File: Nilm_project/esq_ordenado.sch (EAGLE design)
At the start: 37 parts, among them IC1 LM1117IMPX-3.3, J4 10103594-0001LF, Q1 SMD-TRANSISTORS-NPN-25V-500MW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, Q2 SMD-TRANSISTORS-NPN-25V-500MW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, U1 ESP-32S, U2 CP2102-GM, U3 TPD2S017DBVR, U4 SP0503BAHT

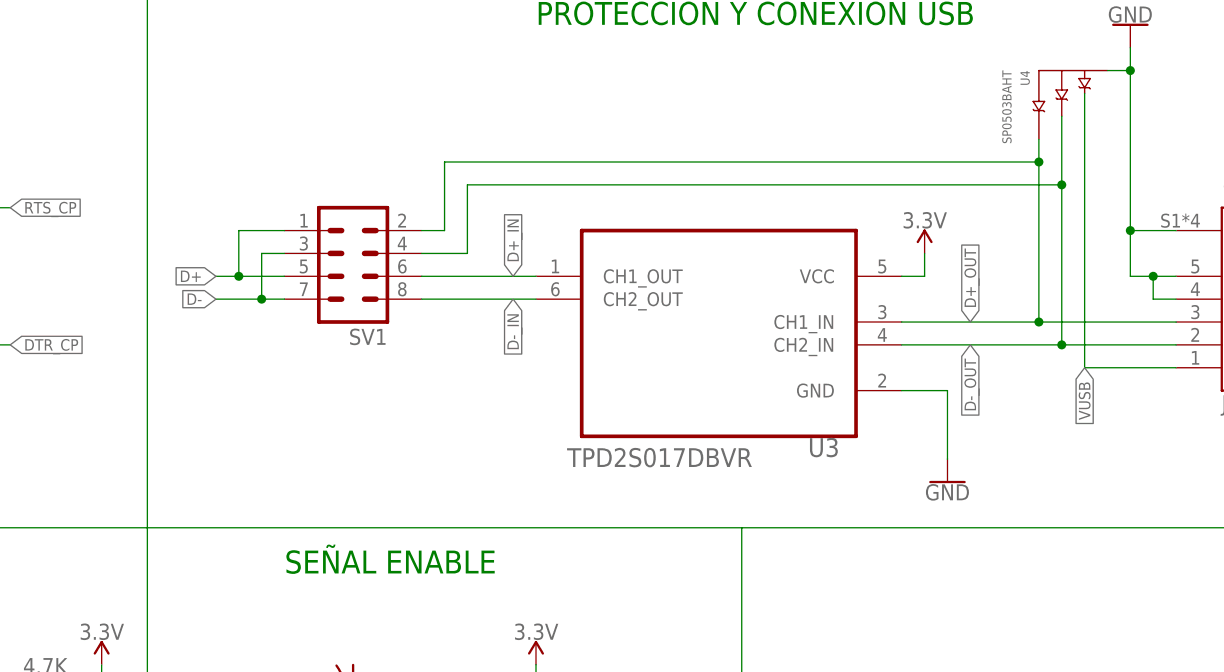
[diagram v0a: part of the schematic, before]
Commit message: Adicionando Datasheet TPD2S017 y conexiones entre D+ y D- a la regleta
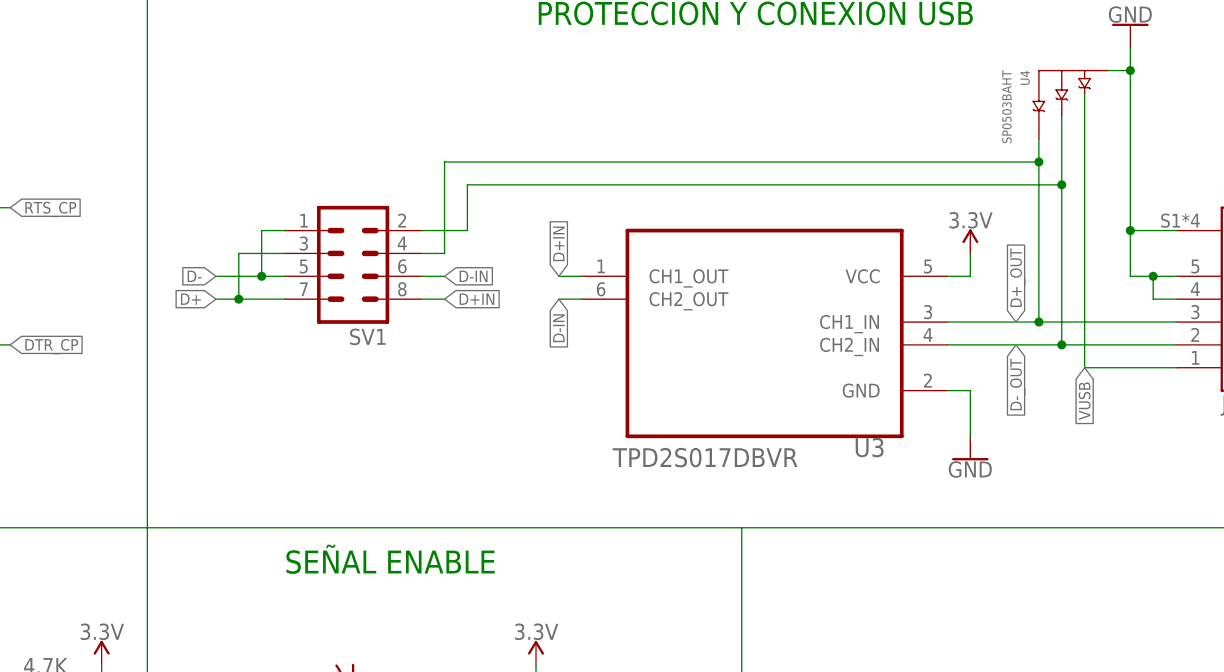
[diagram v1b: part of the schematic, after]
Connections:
- removed net D+_IN: SV1.6, U3.CH1_OUT
- removed net D-_IN: SV1.8, U3.CH2_OUT
- new net D+IN: SV1.8, U3.CH1_OUT
- new net D-IN: SV1.6, U3.CH2_OUT
- net D+: now also SV1.3, SV1.7; no longer SV1.1, SV1.5
- net D+_OUT: now also SV1.4; no longer SV1.2
- net D-: now also SV1.1, SV1.5; no longer SV1.3, SV1.7
- net D-_OUT: now also SV1.2; no longer SV1.4
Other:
- moved on the sheet: U3
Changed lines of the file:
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@@
 <attribute name="NAME" x="214.63" y="189.738" size="1.778" layer="95" rot="R180"/>
 </instance>
-<instance part="U3" gate="A" x="251.46" y="193.04" smashed="yes" rot="MR0">
-<attribute name="NAME" x="264.882759375" y="175.5093" size="2.086959375" layer="95" ratio="10" rot="SMR0"/>
-<attribute name="VALUE" x="255.199990625" y="174.391" size="2.08625" layer="96" ratio="10" rot="SMR0"/>
+<instance part="U3" gate="A" x="256.54" y="193.04" smashed="yes" rot="MR0">
+<attribute name="NAME" x="269.962759375" y="175.5093" size="2.086959375" layer="95" ratio="10" rot="SMR0"/>
+<attribute name="VALUE" x="260.279990625" y="174.391" size="2.08625" layer="96" ratio="10" rot="SMR0"/>
 </instance>
 <instance part="U4" gate="G$1" x="289.56" y="215.9" smashed="yes" rot="R180">
@@
 <attribute name="VALUE" x="282.9587" y="218.460509375" size="1.0162" layer="96" rot="R270"/>
 </instance>
-<instance part="SUPPLY10" gate="G$1" x="274.32" y="198.12" smashed="yes">
-<attribute name="VALUE" x="274.32" y="200.914" size="1.778" layer="96" align="bottom-center"/>
-</instance>
-<instance part="GND21" gate="1" x="276.86" y="172.72" smashed="yes">
-<attribute name="VALUE" x="276.86" y="172.466" size="1.778" layer="96" align="top-center"/>
+<instance part="SUPPLY10" gate="G$1" x="279.4" y="198.12" smashed="yes">
+<attribute name="VALUE" x="279.4" y="200.914" size="1.778" layer="96" align="bottom-center"/>
+</instance>
+<instance part="GND21" gate="1" x="279.4" y="175.26" smashed="yes">
+<attribute name="VALUE" x="279.4" y="175.006" size="1.778" layer="96" align="top-center"/>
 </instance>
 <instance part="GND22" gate="1" x="297.18" y="223.52" smashed="yes" rot="R180">
@@
 <segment>
 <pinref part="U3" gate="A" pin="VCC"/>
-<wire x1="271.78" y1="195.58" x2="274.32" y2="195.58" width="0.1524" layer="91"/>
-<wire x1="274.32" y1="195.58" x2="274.32" y2="198.12" width="0.1524" layer="91"/>
+<wire x1="276.86" y1="195.58" x2="279.4" y2="195.58" width="0.1524" layer="91"/>
+<wire x1="279.4" y1="195.58" x2="279.4" y2="198.12" width="0.1524" layer="91"/>
 <pinref part="SUPPLY10" gate="G$1" pin="3.3V"/>
 </segment>
@@
 <segment>
 <pinref part="U3" gate="A" pin="GND"/>
-<wire x1="271.78" y1="182.88" x2="276.86" y2="182.88" width="0.1524" layer="91"/>
-<wire x1="276.86" y1="182.88" x2="276.86" y2="175.26" width="0.1524" layer="91"/>
+<wire x1="276.86" y1="182.88" x2="279.4" y2="182.88" width="0.1524" layer="91"/>
+<wire x1="279.4" y1="182.88" x2="279.4" y2="177.8" width="0.1524" layer="91"/>
 <pinref part="GND21" gate="1" pin="GND"/>
 </segment>
@@
 </segment>
 <segment>
-<pinref part="SV1" gate="G$1" pin="5"/>
-<wire x1="203.2" y1="195.58" x2="198.12" y2="195.58" width="0.1524" layer="91"/>
-<label x="195.58" y="195.58" size="1.27" layer="95" rot="MR0" xref="yes"/>
-<pinref part="SV1" gate="G$1" pin="1"/>
-<wire x1="198.12" y1="195.58" x2="195.58" y2="195.58" width="0.1524" layer="91"/>
-<wire x1="198.12" y1="195.58" x2="198.12" y2="200.66" width="0.1524" layer="91"/>
-<wire x1="198.12" y1="200.66" x2="203.2" y2="200.66" width="0.1524" layer="91"/>
-<junction x="198.12" y="195.58"/>
+<label x="195.58" y="193.04" size="1.27" layer="95" rot="MR0" xref="yes"/>
+<wire x1="198.12" y1="193.04" x2="195.58" y2="193.04" width="0.1524" layer="91"/>
+<wire x1="198.12" y1="193.04" x2="198.12" y2="198.12" width="0.1524" layer="91"/>
+<pinref part="SV1" gate="G$1" pin="3"/>
+<wire x1="198.12" y1="198.12" x2="203.2" y2="198.12" width="0.1524" layer="91"/>
+<pinref part="SV1" gate="G$1" pin="7"/>
+<wire x1="198.12" y1="193.04" x2="203.2" y2="193.04" width="0.1524" layer="91"/>
+<junction x="198.12" y="193.04"/>
 </segment>
 </net>
@@
 </segment>
 <segment>
-<pinref part="SV1" gate="G$1" pin="7"/>
-<wire x1="203.2" y1="193.04" x2="200.66" y2="193.04" width="0.1524" layer="91"/>
-<label x="195.58" y="193.04" size="1.27" layer="95" rot="MR0" xref="yes"/>
-<wire x1="200.66" y1="193.04" x2="195.58" y2="193.04" width="0.1524" layer="91"/>
-<wire x1="200.66" y1="193.04" x2="200.66" y2="198.12" width="0.1524" layer="91"/>
-<junction x="200.66" y="193.04"/>
-<pinref part="SV1" gate="G$1" pin="3"/>
-<wire x1="200.66" y1="198.12" x2="203.2" y2="198.12" width="0.1524" layer="91"/>
-</segment>
-</net>
-<net name="D+_IN" class="0">
-<segment>
-<pinref part="U3" gate="A" pin="CH1_OUT"/>
-<pinref part="SV1" gate="G$1" pin="6"/>
-<wire x1="231.14" y1="195.58" x2="218.44" y2="195.58" width="0.1524" layer="91"/>
-<label x="228.6" y="195.58" size="1.27" layer="95" rot="R90" xref="yes"/>
-</segment>
-</net>
-<net name="D-_IN" class="0">
-<segment>
-<pinref part="U3" gate="A" pin="CH2_OUT"/>
-<pinref part="SV1" gate="G$1" pin="8"/>
-<wire x1="231.14" y1="193.04" x2="218.44" y2="193.04" width="0.1524" layer="91"/>
-<label x="228.6" y="193.04" size="1.27" layer="95" rot="R270" xref="yes"/>
+<label x="195.58" y="195.58" size="1.27" layer="95" rot="MR0" xref="yes"/>
+<wire x1="200.66" y1="195.58" x2="195.58" y2="195.58" width="0.1524" layer="91"/>
+<wire x1="200.66" y1="195.58" x2="200.66" y2="200.66" width="0.1524" layer="91"/>
+<pinref part="SV1" gate="G$1" pin="1"/>
+<wire x1="200.66" y1="200.66" x2="203.2" y2="200.66" width="0.1524" layer="91"/>
+<pinref part="SV1" gate="G$1" pin="5"/>
+<wire x1="200.66" y1="195.58" x2="203.2" y2="195.58" width="0.1524" layer="91"/>
+<junction x="200.66" y="195.58"/>
 </segment>
 </net>
@@
 <segment>
 <pinref part="U3" gate="A" pin="CH1_IN"/>
-<wire x1="271.78" y1="190.5" x2="287.02" y2="190.5" width="0.1524" layer="91"/>
+<wire x1="276.86" y1="190.5" x2="287.02" y2="190.5" width="0.1524" layer="91"/>
 <pinref part="U4" gate="G$1" pin="C"/>
 <wire x1="287.02" y1="190.5" x2="302.26" y2="190.5" width="0.1524" layer="91"/>
 <wire x1="287.02" y1="210.82" x2="287.02" y2="208.28" width="0.1524" layer="91"/>
 <junction x="287.02" y="190.5"/>
-<pinref part="SV1" gate="G$1" pin="2"/>
 <wire x1="287.02" y1="208.28" x2="287.02" y2="190.5" width="0.1524" layer="91"/>
-<wire x1="218.44" y1="200.66" x2="220.98" y2="200.66" width="0.1524" layer="91"/>
-<wire x1="220.98" y1="200.66" x2="220.98" y2="208.28" width="0.1524" layer="91"/>
+<wire x1="220.98" y1="198.12" x2="220.98" y2="208.28" width="0.1524" layer="91"/>
 <wire x1="220.98" y1="208.28" x2="287.02" y2="208.28" width="0.1524" layer="91"/>
 <junction x="287.02" y="208.28"/>
 <pinref part="J4" gate="G$1" pin="3"/>
-<label x="279.4" y="190.5" size="1.27" layer="95" rot="R90" xref="yes"/>
+<label x="284.48" y="190.5" size="1.27" layer="95" rot="R90" xref="yes"/>
+<pinref part="SV1" gate="G$1" pin="4"/>
+<wire x1="220.98" y1="198.12" x2="218.44" y2="198.12" width="0.1524" layer="91"/>
 </segment>
 </net>
@@
 <pinref part="J4" gate="G$1" pin="2"/>
 <pinref part="U3" gate="A" pin="CH2_IN"/>
-<wire x1="271.78" y1="187.96" x2="289.56" y2="187.96" width="0.1524" layer="91"/>
+<wire x1="276.86" y1="187.96" x2="289.56" y2="187.96" width="0.1524" layer="91"/>
 <pinref part="U4" gate="G$1" pin="B"/>
 <wire x1="289.56" y1="187.96" x2="302.26" y2="187.96" width="0.1524" layer="91"/>
 <wire x1="289.56" y1="213.36" x2="289.56" y2="205.74" width="0.1524" layer="91"/>
 <junction x="289.56" y="187.96"/>
-<pinref part="SV1" gate="G$1" pin="4"/>
 <wire x1="289.56" y1="205.74" x2="289.56" y2="187.96" width="0.1524" layer="91"/>
-<wire x1="218.44" y1="198.12" x2="223.52" y2="198.12" width="0.1524" layer="91"/>
-<wire x1="223.52" y1="198.12" x2="223.52" y2="205.74" width="0.1524" layer="91"/>
 <wire x1="223.52" y1="205.74" x2="289.56" y2="205.74" width="0.1524" layer="91"/>
 <junction x="289.56" y="205.74"/>
-<label x="279.4" y="187.96" size="1.27" layer="95" rot="R270" xref="yes"/>
+<label x="284.48" y="187.96" size="1.27" layer="95" rot="R270" xref="yes"/>
+<pinref part="SV1" gate="G$1" pin="2"/>
+<wire x1="218.44" y1="200.66" x2="223.52" y2="200.66" width="0.1524" layer="91"/>
+<wire x1="223.52" y1="200.66" x2="223.52" y2="205.74" width="0.1524" layer="91"/>
 </segment>
 </net>
@@
 </segment>
 </net>
+<net name="D-IN" class="0">
+<segment>
+<pinref part="SV1" gate="G$1" pin="6"/>
+<wire x1="218.44" y1="195.58" x2="220.98" y2="195.58" width="0.1524" layer="91"/>
+<label x="220.98" y="195.58" size="1.27" layer="95" xref="yes"/>
+</segment>
+<segment>
+<pinref part="U3" gate="A" pin="CH2_OUT"/>
+<wire x1="236.22" y1="193.04" x2="233.68" y2="193.04" width="0.1524" layer="91"/>
+<label x="233.68" y="193.04" size="1.27" layer="95" rot="R270" xref="yes"/>
+</segment>
+</net>
+<net name="D+IN" class="0">
+<segment>
+<pinref part="SV1" gate="G$1" pin="8"/>
+<wire x1="218.44" y1="193.04" x2="220.98" y2="193.04" width="0.1524" layer="91"/>
+<label x="220.98" y="193.04" size="1.27" layer="95" xref="yes"/>
+</segment>
+<segment>
+<pinref part="U3" gate="A" pin="CH1_OUT"/>
+<wire x1="236.22" y1="195.58" x2="233.68" y2="195.58" width="0.1524" layer="91"/>
+<label x="233.68" y="195.58" size="1.27" layer="95" rot="R90" xref="yes"/>
+</segment>
+</net>

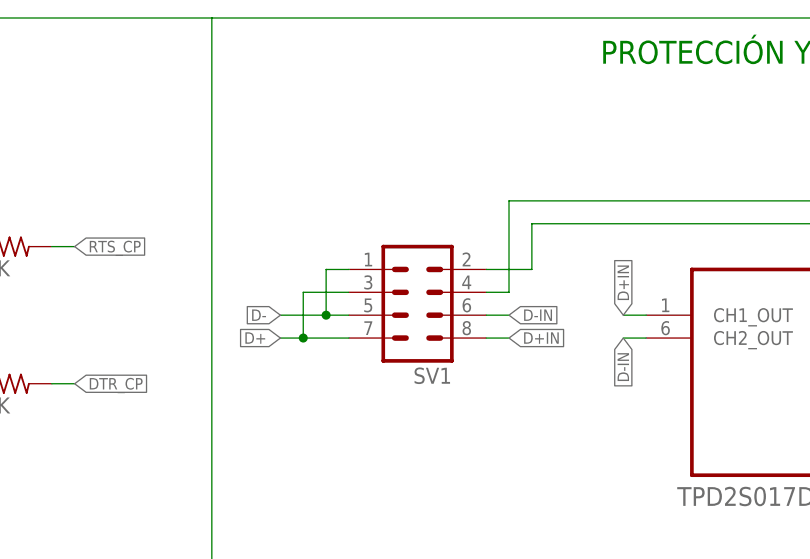
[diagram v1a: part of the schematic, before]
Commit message: Correcciones D+ Y D- en TPD2S017 y en los pines, para un mejor ruteo
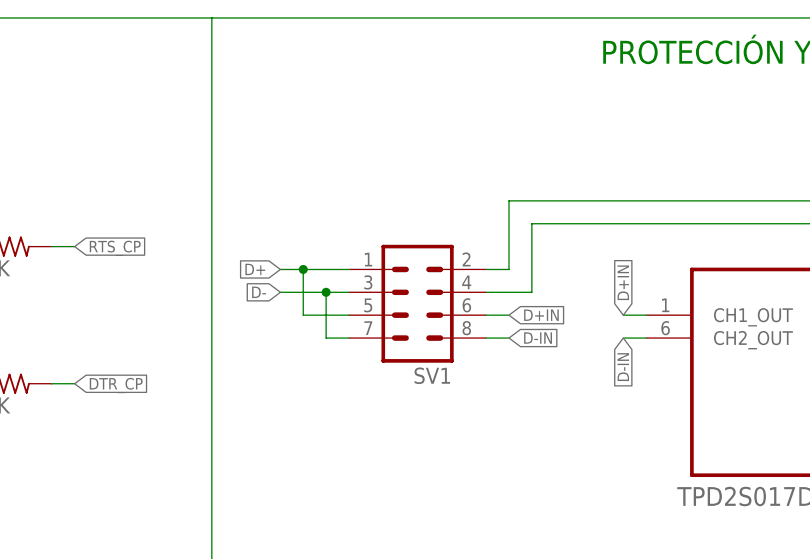
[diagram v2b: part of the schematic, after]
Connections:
- net D+: now also SV1.1, SV1.5; no longer SV1.3, SV1.7
- net D+IN: now also SV1.6; no longer SV1.8
- net D+_OUT: now also SV1.2; no longer SV1.4
- net D-: now also SV1.3, SV1.7; no longer SV1.1, SV1.5
- net D-IN: now also SV1.8; no longer SV1.6
- net D-_OUT: now also SV1.4; no longer SV1.2
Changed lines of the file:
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@@
 </segment>
 <segment>
-<label x="195.58" y="193.04" size="1.27" layer="95" rot="MR0" xref="yes"/>
-<wire x1="198.12" y1="193.04" x2="195.58" y2="193.04" width="0.1524" layer="91"/>
-<wire x1="198.12" y1="193.04" x2="198.12" y2="198.12" width="0.1524" layer="91"/>
-<pinref part="SV1" gate="G$1" pin="3"/>
-<wire x1="198.12" y1="198.12" x2="203.2" y2="198.12" width="0.1524" layer="91"/>
-<pinref part="SV1" gate="G$1" pin="7"/>
-<wire x1="198.12" y1="193.04" x2="203.2" y2="193.04" width="0.1524" layer="91"/>
-<junction x="198.12" y="193.04"/>
+<label x="195.58" y="200.66" size="1.27" layer="95" rot="MR0" xref="yes"/>
+<pinref part="SV1" gate="G$1" pin="1"/>
+<wire x1="195.58" y1="200.66" x2="198.12" y2="200.66" width="0.1524" layer="91"/>
+<pinref part="SV1" gate="G$1" pin="5"/>
+<wire x1="198.12" y1="200.66" x2="203.2" y2="200.66" width="0.1524" layer="91"/>
+<wire x1="198.12" y1="200.66" x2="198.12" y2="195.58" width="0.1524" layer="91"/>
+<wire x1="198.12" y1="195.58" x2="203.2" y2="195.58" width="0.1524" layer="91"/>
+<junction x="198.12" y="200.66"/>
 </segment>
 </net>
@@
 </segment>
 <segment>
-<label x="195.58" y="195.58" size="1.27" layer="95" rot="MR0" xref="yes"/>
-<wire x1="200.66" y1="195.58" x2="195.58" y2="195.58" width="0.1524" layer="91"/>
-<wire x1="200.66" y1="195.58" x2="200.66" y2="200.66" width="0.1524" layer="91"/>
-<pinref part="SV1" gate="G$1" pin="1"/>
-<wire x1="200.66" y1="200.66" x2="203.2" y2="200.66" width="0.1524" layer="91"/>
-<pinref part="SV1" gate="G$1" pin="5"/>
-<wire x1="200.66" y1="195.58" x2="203.2" y2="195.58" width="0.1524" layer="91"/>
-<junction x="200.66" y="195.58"/>
+<label x="195.58" y="198.12" size="1.27" layer="95" rot="MR0" xref="yes"/>
+<pinref part="SV1" gate="G$1" pin="3"/>
+<wire x1="195.58" y1="198.12" x2="200.66" y2="198.12" width="0.1524" layer="91"/>
+<pinref part="SV1" gate="G$1" pin="7"/>
+<wire x1="200.66" y1="198.12" x2="203.2" y2="198.12" width="0.1524" layer="91"/>
+<wire x1="200.66" y1="198.12" x2="200.66" y2="193.04" width="0.1524" layer="91"/>
+<wire x1="200.66" y1="193.04" x2="203.2" y2="193.04" width="0.1524" layer="91"/>
+<junction x="200.66" y="198.12"/>
 </segment>
 </net>
@@
 <junction x="287.02" y="190.5"/>
 <wire x1="287.02" y1="208.28" x2="287.02" y2="190.5" width="0.1524" layer="91"/>
-<wire x1="220.98" y1="198.12" x2="220.98" y2="208.28" width="0.1524" layer="91"/>
 <wire x1="220.98" y1="208.28" x2="287.02" y2="208.28" width="0.1524" layer="91"/>
 <junction x="287.02" y="208.28"/>
 <pinref part="J4" gate="G$1" pin="3"/>
 <label x="284.48" y="190.5" size="1.27" layer="95" rot="R90" xref="yes"/>
-<pinref part="SV1" gate="G$1" pin="4"/>
-<wire x1="220.98" y1="198.12" x2="218.44" y2="198.12" width="0.1524" layer="91"/>
+<pinref part="SV1" gate="G$1" pin="2"/>
+<wire x1="220.98" y1="208.28" x2="220.98" y2="200.66" width="0.1524" layer="91"/>
+<wire x1="220.98" y1="200.66" x2="218.44" y2="200.66" width="0.1524" layer="91"/>
 </segment>
 </net>
@@
 <junction x="289.56" y="205.74"/>
 <label x="284.48" y="187.96" size="1.27" layer="95" rot="R270" xref="yes"/>
-<pinref part="SV1" gate="G$1" pin="2"/>
-<wire x1="218.44" y1="200.66" x2="223.52" y2="200.66" width="0.1524" layer="91"/>
-<wire x1="223.52" y1="200.66" x2="223.52" y2="205.74" width="0.1524" layer="91"/>
+<wire x1="223.52" y1="198.12" x2="223.52" y2="205.74" width="0.1524" layer="91"/>
+<pinref part="SV1" gate="G$1" pin="4"/>
+<wire x1="223.52" y1="198.12" x2="218.44" y2="198.12" width="0.1524" layer="91"/>
 </segment>
 </net>
@@
 <net name="D-IN" class="0">
 <segment>
-<pinref part="SV1" gate="G$1" pin="6"/>
-<wire x1="218.44" y1="195.58" x2="220.98" y2="195.58" width="0.1524" layer="91"/>
-<label x="220.98" y="195.58" size="1.27" layer="95" xref="yes"/>
-</segment>
-<segment>
 <pinref part="U3" gate="A" pin="CH2_OUT"/>
 <wire x1="236.22" y1="193.04" x2="233.68" y2="193.04" width="0.1524" layer="91"/>
 <label x="233.68" y="193.04" size="1.27" layer="95" rot="R270" xref="yes"/>
 </segment>
-</net>
-<net name="D+IN" class="0">
 <segment>
 <pinref part="SV1" gate="G$1" pin="8"/>
@@
 <label x="220.98" y="193.04" size="1.27" layer="95" xref="yes"/>
 </segment>
+</net>
+<net name="D+IN" class="0">
 <segment>
 <pinref part="U3" gate="A" pin="CH1_OUT"/>
@@
 <label x="233.68" y="195.58" size="1.27" layer="95" rot="R90" xref="yes"/>
 </segment>
+<segment>
+<pinref part="SV1" gate="G$1" pin="6"/>
+<wire x1="218.44" y1="195.58" x2="220.98" y2="195.58" width="0.1524" layer="91"/>
+<label x="220.98" y="195.58" size="1.27" layer="95" xref="yes"/>
+</segment>
 </net>
